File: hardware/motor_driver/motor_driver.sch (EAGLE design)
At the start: 88 parts

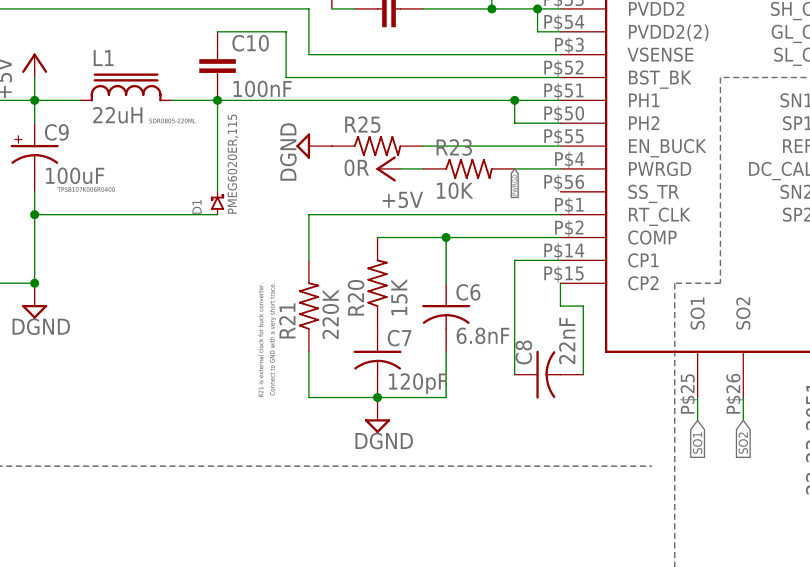
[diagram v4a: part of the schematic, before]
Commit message: Routed mosfets
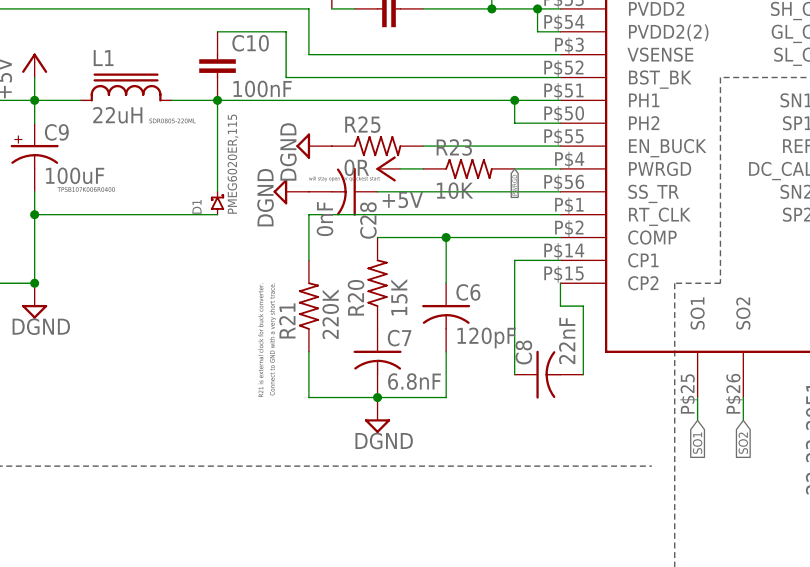
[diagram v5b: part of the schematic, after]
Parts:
- added C28: 0nF, adafruit:C-USC0603
- C6: value 6.8nF -> 120pF
- C7: value 120pF -> 6.8nF
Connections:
- new net N$9: C28.1, U$7.SS_TR
- net DGND: now also C28.2
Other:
- note added: "will stay open for quickest start"
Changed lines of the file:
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@@
 <part name="R23" library="adafruit" deviceset="R-US_" device="R0603" value="10K"/>
 <part name="R24" library="adafruit" deviceset="R-US_" device="R0603" value="18K"/>
-<part name="C6" library="adafruit" deviceset="C-US" device="C0603" value="6.8nF"/>
-<part name="C7" library="adafruit" deviceset="C-US" device="C0603" value="120pF"/>
+<part name="C6" library="adafruit" deviceset="C-US" device="C0603" value="120pF"/>
+<part name="C7" library="adafruit" deviceset="C-US" device="C0603" value="6.8nF"/>
 <part name="C8" library="adafruit" deviceset="C-US" device="C0603" value="22nF"/>
 <part name="SUPPLY9" library="supply2" deviceset="DGND" device=""/>
@@
 <part name="SUPPLY27" library="supply2" deviceset="GND" device=""/>
 <part name="SUPPLY13" library="supply2" deviceset="DGND" device=""/>
+<part name="C28" library="adafruit" deviceset="C-US" device="C0603" value="0nF"/>
+<part name="SUPPLY28" library="supply2" deviceset="DGND" device=""/>
 </parts>
 <sheets>
@@
 <wire x1="114.3" y1="-101.6" x2="88.9" y2="-101.6" width="0.1524" layer="97" style="shortdash"/>
 <wire x1="88.9" y1="-101.6" x2="88.9" y2="-88.9" width="0.1524" layer="97" style="shortdash"/>
+<text x="198.12" y="-39.37" size="0.4064" layer="97">will stay open for quickest start</text>
 </plain>
 <instances>
@@
 <instance part="SUPPLY27" gate="GND" x="269.24" y="-12.7" rot="R90"/>
 <instance part="SUPPLY13" gate="G$1" x="200.66" y="-17.78" rot="R180"/>
+<instance part="C28" gate="G$1" x="203.2" y="-40.64" rot="R270"/>
+<instance part="SUPPLY28" gate="G$1" x="195.58" y="-40.64" rot="R270"/>
 </instances>
 <busses>
@@
 <pinref part="SUPPLY13" gate="G$1" pin="DGND"/>
 </segment>
+<segment>
+<pinref part="C28" gate="G$1" pin="2"/>
+<pinref part="SUPPLY28" gate="G$1" pin="DGND"/>
+</segment>
 </net>
 <net name="+5V" class="0">
@@
 </segment>
 </net>
+<net name="N$9" class="0">
+<segment>
+<pinref part="C28" gate="G$1" pin="1"/>
+<pinref part="U$7" gate="G$1" pin="SS_TR"/>
+<wire x1="205.74" y1="-40.64" x2="226.06" y2="-40.64" width="0.1524" layer="91"/>
+</segment>
+</net>
